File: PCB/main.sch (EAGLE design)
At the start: 38 parts, among them X1 BU-SMA-V

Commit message: Eagle Schematic From Lab
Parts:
- removed LSP1, LSP2: LSP10, solpad:LSP10
- added AUX-L, AUX-R, L-OUT, R-OUT, REC-L, REC-R: LSP10, solpad:LSP10
- added R10, R8, R9: 330, resistor:R-EU_M0805
- added R11, R12: 10k, resistor:R-EU_M0805
- added U$4, U$5: MAX4586, MAX4586:MAX4586
- JP4: device pinhead:PINHD-2X9 -> pinhead:PINHD-1X16
- renumbered LSP6 to V+, LSP7 to V-
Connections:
- net N$12 renamed D5
- net N$55 renamed V+
- removed net L-OUT: JP2.3, R7.1, U$1.L-OUT
- removed net N$14: JP4.16, U$2.RD7/SEG7
- removed net N$15: JP4.1, U$2.RF7/~SS/SEG25
- removed net N$16: JP4.3, U$2.RF6/AN11/SEG24
- removed net N$17: JP4.5, U$2.RF5/AN10/CVREF/SEG23
- removed net N$18: JP4.7, U$2.RF4/AN9/SEG22
- removed net N$19: JP4.9, U$2.RF3/AN8/SEG21
- removed net N$20: JP4.11, U$2.RF2/AN7/C1OUT/SEG20
- removed net N$21: JP4.13, U$2.RF1/AN6/C2OUT/SEG19
- removed net N$22: JP4.15, U$2.RF0/AN5/SEG18
- removed net N$5 (its old number): JP4.4, U$2.RD1/SEG1
- removed net N$52: JP9.3, U$2.RE6/COM3
- removed net N$53: JP9.4, U$2.RE7/CCP2/SEG31
- removed net N$54: U$2.COM0
- removed net N$57: R4.1, U$4.1.+IN
- removed net N$60: C6.1, C7.1, LSP1.MP
- removed net N$62: R7.2, U$4.2.+IN
- removed net N$64: C10.1, C9.1, LSP2.MP
- removed net N$67: JP1.2, R2.1, U$1.DATA
- removed net N$68: JP1.3, R1.1, U$1.CLOCK
- removed net N$7 (its old number): JP4.8, U$2.RD3/SEG3
- removed net R-OUT: JP2.2, R4.2, U$1.R-OUT
- new net AMP-L: U$4.COM
- new net AMP-R: U$5.COM
- new net AUX-L: AUX-L.MP, U$4.NO3
- new net AUX-R: AUX-R.MP, U$5.NO3
- new net COM0: JP9.1, U$2.COM0
- new net D0: JP4.7, U$2.RD0/SEG0
- new net D1: JP4.8, U$2.RD1/SEG1
- new net D2: JP4.9, U$2.RD2/SEG2
- new net D3: JP4.10
- new net D4: JP4.11, U$2.RD4/SEG4
- new net D6: JP4.13, U$2.RD6/SEG6
- new net D7: JP4.14, U$2.RD7/SEG7
- new net E: JP4.6, JP9.4, U$2.RE6/COM3
- new net FM-L: JP2.3, U$1.L-OUT, U$4.NO1
- new net FM-R: JP2.2, U$1.R-OUT, U$5.NO1
- new net REC-L: REC-L.MP, U$4.NO2
- new net REC-R: REC-R.MP, U$5.NO2
- new net RS: JP4.4, JP9.5, U$2.RE7/CCP2/SEG31
- net +3V3: now also JP4.2, R8.1, R9.2, U$4.A, U$4.V+, U$5.V+; no longer JP4.17
- net GND: now also JP4.1, JP4.16, JP4.5, R10.1, U$4.GND, U$5.A, U$5.GND; no longer JP4.18
- net N$13: now also JP4.3, R10.2, R9.1; no longer JP4.14, U$2.RD6/SEG6
- net N$2: now also JP4.15, R8.2; no longer JP4.2, U$2.RD0/SEG0
- net N$50: now also JP9.2; no longer JP9.1
- net N$51: now also JP9.3; no longer JP9.2
- net N$6: now also C10.1, C9.1, L-OUT.MP; no longer JP4.6, U$2.RD2/SEG2
- net N$8: now also C6.1, C7.1, R-OUT.MP; no longer JP4.10, U$2.RD4/SEG4
- net SCL: now also JP1.3, R1.1, U$1.CLOCK, U$4.SCL, U$5.SCL
- net SDA: now also JP1.2, R2.1, U$1.DATA, U$4.SDA, U$5.SDA
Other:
- note removed: "LCD screen"
- note removed: "Lout"
- note removed: "Rout"
- moved on the sheet: C1, C10, C2, C5, C6, C7, C8, C9, JP1, JP2, JP6, JP8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

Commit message: Eagle Schematic Changes
Pins numbers added
IC names added
Text re-aligned
Amp corrected
Components re-named
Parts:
- removed JP1, JP2: (no value), pinhead:PINHD-1X3
- removed JP3: (no value), pinhead:PINHD-1X6
- removed JP4: (no value), pinhead:PINHD-1X16
- removed JP5, JP6, JP7, JP8, JP9: (no value), pinhead:PINHD-1X8
- removed U$1: AR1010, ar1010:AR1010
- removed U$4.: TDA2822D, linear:TDA2822D
- removed U$5: MAX4586, MAX4586:MAX4586
- added AMP-: TDA2822D, linear:TDA2822D
- added H1: (no value), pinhead:PINHD-1X16
- added H2, H4, H5, H6, H7: (no value), pinhead:PINHD-1X8
- added H3: (no value), pinhead:PINHD-1X6
- added H8, H9: (no value), pinhead:PINHD-1X3
- added MICROCONTROLLER: PIC18F6490-I/PT, Microchip_By_element14_Batch_1:PIC18F6490-I/PT
- added VOLTAGE_REGULATOR: MCP1700T-1802E/TT, mcp1700t-vreg:MCP1700T-1802E/TT
- R11, R12: value 10k -> 330
- R4, R7: value 10k -> 100k
- R5: value 4.7 -> 10k
- R8: value 330 -> 10k
- R9: value 330 -> 4.7
- U$2: value PIC18F6490-I/PT -> AR1010; device Microchip_By_element14_Batch_1:PIC18F6490-I/PT -> ar1010:AR1010; VAL (none) -> AR1010
- U$3: value MCP1700T-1802E/TT -> MAX4586; device mcp1700t-vreg:MCP1700T-1802E/TT -> MAX4586:MAX4586; VAL (none) -> MAX4586
- U$4: VAL (none) -> MAX4586
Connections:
- removed net N$58: C5.1, U$4.1.-IN
- removed net N$65: C10.2, R6.1
- removed net N$66: C8.1, U$4.2.-IN
- new net N$12: AMP-R.-IN, C5.1
- new net N$14: AMP-L.-IN, C8.1
- new net N$16: C10.2, R9.2
- new net N$17: AMP-L.+IN, R7.2, R8.2
- new net N$8: AMP-R.+IN, R4.1, R5.2
- net +3V3: now also H1.2, H3.2, MICROCONTROLLER.AVDD, MICROCONTROLLER.VDD, MICROCONTROLLER.VDD_2, MICROCONTROLLER.VDD_3, MICROCONTROLLER.VDD_4, R10.1, R11.2, U$2.VCC, U$3.NO2, U$4.NO2, U$4.NO3, VOLTAGE_REGULATOR.VOUT; no longer JP3.2, JP4.2, R8.1, R9.2, U$1.VCC, U$2.AVDD, U$2.VDD, U$2.VDD_2, U$2.VDD_3, U$2.VDD_4, U$3.VOUT, U$4.A, U$4.V+, U$5.V+
- net AMP-L: now also R7.1, U$4.NO4; no longer U$4.COM
- net AMP-R: now also R4.2, U$3.NO4; no longer U$5.COM
- net AUX-L: now also U$4.A; no longer U$4.NO3
- net AUX-R: now also U$3.A; no longer U$5.NO3
- net COM0: now also H7.1, MICROCONTROLLER.COM0; no longer JP9.1, U$2.COM0
- net D0: now also H1.7, MICROCONTROLLER.RD0/SEG0; no longer JP4.7, U$2.RD0/SEG0
- net D1: now also H1.8, MICROCONTROLLER.RD1/SEG1; no longer JP4.8, U$2.RD1/SEG1
- net D2: now also H1.9, MICROCONTROLLER.RD2/SEG2; no longer JP4.9, U$2.RD2/SEG2
- net D3: now also H1.10, MICROCONTROLLER.RD3/SEG3; no longer JP4.10
- net D4: now also H1.11, MICROCONTROLLER.RD4/SEG4; no longer JP4.11, U$2.RD4/SEG4
- net D5: now also H1.12, MICROCONTROLLER.RD5/SEG5; no longer JP4.12, U$2.RD5/SEG5
- net D6: now also H1.13, MICROCONTROLLER.RD6/SEG6; no longer JP4.13, U$2.RD6/SEG6
- net D7: now also H1.14, MICROCONTROLLER.RD7/SEG7; no longer JP4.14, U$2.RD7/SEG7
- net E: now also H1.6, H7.4, MICROCONTROLLER.RE6/COM3; no longer JP4.6, JP9.4, U$2.RE6/COM3
- net FM-L: now also H8.3, U$2.L-OUT, U$4.SCL; no longer JP2.3, U$1.L-OUT, U$4.NO1
- net FM-R: now also H8.2, U$2.R-OUT, U$3.SCL; no longer JP2.2, U$1.R-OUT, U$5.NO1
- net GND: now also AMP-R.V-, H1.1, H1.16, H1.5, H3.3, H8.1, H9.1, MICROCONTROLLER.AVSS, MICROCONTROLLER.VSS, MICROCONTROLLER.VSS_2, MICROCONTROLLER.VSS_3, MICROCONTROLLER.VSS_4, R12.1, R6.1, R8.1, R9.1, U$2.BUSMODE, U$2.GND, U$3.NO3, U$3.SDA, U$4.SDA, VOLTAGE_REGULATOR.GND; no longer JP1.1, JP2.1, JP3.3, JP4.1, JP4.16, JP4.5, R10.1, R6.2, U$1.BUSMODE, U$1.GND, U$2.AVSS, U$2.VSS, U$2.VSS_2, U$2.VSS_3, U$2.VSS_4, U$3.GND, U$4.1.V-, U$4.GND, U$5.A, U$5.GND
- net N$1: now also H3.1, MICROCONTROLLER.RG5/~MCLR/VPP; no longer JP3.1, U$2.RG5/~MCLR/VPP
- net N$10: now also H3.5, H6.7, MICROCONTROLLER.RB6/KBI2/PGC; no longer JP3.5, JP5.7, U$2.RB6/KBI2/PGC
- net N$11: now also H3.4, H6.8, MICROCONTROLLER.RB7/KBI3/PGD; no longer JP3.4, JP5.8, U$2.RB7/KBI3/PGD
- net N$13: now also H1.3, R11.1, R12.2; no longer JP4.3, R10.2, R9.1
- net N$2: now also H1.15, R10.2; no longer JP4.15, R8.2
- net N$23: now also H5.8, MICROCONTROLLER.RC7/RX1/DT1; no longer JP6.8, U$2.RC7/RX1/DT1
- net N$24: now also H5.7, MICROCONTROLLER.RC6/TX1/CK1; no longer JP6.7, U$2.RC6/TX1/CK1
- net N$25: now also H6.5, MICROCONTROLLER.RB4/KBI0/SEG11; no longer JP5.5, U$2.RB4/KBI0/SEG11
- net N$26: now also H6.4, MICROCONTROLLER.RB3/INT3/SEG10; no longer JP5.4, U$2.RB3/INT3/SEG10
- net N$27: now also H6.3, MICROCONTROLLER.RB2/INT2/SEG9; no longer JP5.3, U$2.RB2/INT2/SEG9
- net N$28: now also H6.2, MICROCONTROLLER.RB1/INT1/SEG8; no longer JP5.2, U$2.RB1/INT1/SEG8
- net N$29: now also H6.1, MICROCONTROLLER.RB0/INT0; no longer JP5.1, U$2.RB0/INT0
- net N$3: now also U$2.W/R; no longer U$1.W/R
- net N$30: now also H5.6, MICROCONTROLLER.RC5/SDO/SEG12; no longer JP6.6, U$2.RC5/SDO/SEG12
- net N$31: now also H5.3, MICROCONTROLLER.RC2/CCP1/SEG13; no longer JP6.3, U$2.RC2/CCP1/SEG13
- net N$32: now also H5.2, MICROCONTROLLER.RC1/T1OSI/CCP2; no longer JP6.2, U$2.RC1/T1OSI/CCP2
- net N$33: now also H5.1, MICROCONTROLLER.RC0/T1OSO/T13CKI; no longer JP6.1, U$2.RC0/T1OSO/T13CKI
- net N$34: now also H4.8, MICROCONTROLLER.OSC1/CLKI/RA7; no longer JP7.8, U$2.OSC1/CLKI/RA7
- net N$35: now also H4.7, MICROCONTROLLER.OSC2/CLKO/RA6; no longer JP7.7, U$2.OSC2/CLKO/RA6
- net N$36: now also H4.6, MICROCONTROLLER.RA5/AN4/HLVDIN/SEG15; no longer JP7.6, U$2.RA5/AN4/HLVDIN/SEG15
- net N$37: now also H4.5, MICROCONTROLLER.RA4/T0CKI/SEG14; no longer JP7.5, U$2.RA4/T0CKI/SEG14
- net N$38: now also H4.4, MICROCONTROLLER.RA3/AN3/VREF+/SEG17; no longer JP7.4, U$2.RA3/AN3/VREF+/SEG17
- net N$39: now also H4.3, MICROCONTROLLER.RA2/AN2/VREF-/SEG16; no longer JP7.3, U$2.RA2/AN2/VREF-/SEG16
- net N$4: now also U$2.ANT; no longer U$1.ANT
- net N$40: now also H4.2, MICROCONTROLLER.RA1/AN1; no longer JP7.2, U$2.RA1/AN1
- net N$41: now also H4.1, MICROCONTROLLER.RA0/AN0; no longer JP7.1, U$2.RA0/AN0
- net N$42: now also H2.1, MICROCONTROLLER.RG4/SEG26; no longer JP8.1, U$2.RG4/SEG26
- net N$43: now also H2.2, MICROCONTROLLER.RG3/SEG27; no longer JP8.2, U$2.RG3/SEG27
- net N$44: now also H2.3, MICROCONTROLLER.RG2/RX2/DT2/SEG28; no longer JP8.3, U$2.RG2/RX2/DT2/SEG28
- net N$45: now also H2.4, MICROCONTROLLER.RG1/TX2/CK2/SEG29; no longer JP8.4, U$2.RG1/TX2/CK2/SEG29
- net N$46: now also H2.5, MICROCONTROLLER.RG0/SEG30; no longer JP8.5, U$2.RG0/SEG30
- net N$47: now also H2.6, MICROCONTROLLER.LCDBIAS3; no longer JP8.6, U$2.LCDBIAS3
- net N$48: now also H2.7, MICROCONTROLLER.LCDBIAS2; no longer JP8.7, U$2.LCDBIAS2
- net N$49: now also H2.8, MICROCONTROLLER.LCDBIAS1; no longer JP8.8, U$2.LCDBIAS1
- net N$5: now also AMP-L.OUT; no longer U$4.2.OUT
- net N$50: now also H7.2, MICROCONTROLLER.RE4/COM1; no longer JP9.2, U$2.RE4/COM1
- net N$51: now also H7.3, MICROCONTROLLER.RE5/COM2; no longer JP9.3, U$2.RE5/COM2
- net N$61: now also R6.2; no longer R5.2
- net N$7: now also AMP-R.OUT; no longer U$4.1.OUT
- net N$9: now also H6.6, MICROCONTROLLER.RB5/KBI1; no longer JP5.6, U$2.RB5/KBI1
- net REC-L: now also U$4.V+; no longer U$4.NO2
- net REC-R: now also U$3.V+; no longer U$5.NO2
- net RS: now also H1.4, H7.5, MICROCONTROLLER.RE7/CCP2/SEG31; no longer JP4.4, JP9.5, U$2.RE7/CCP2/SEG31
- net SCL: now also H5.4, H9.3, MICROCONTROLLER.RC3/SCK/SCL, U$2.CLOCK, U$3.NO1, U$4.NO1; no longer JP1.3, JP6.4, U$1.CLOCK, U$2.RC3/SCK/SCL, U$4.SCL, U$5.SCL
- net SDA: now also H5.5, H9.2, MICROCONTROLLER.RC4/SDI/SDA, U$2.DATA, U$3.GND, U$4.GND; no longer JP1.2, JP6.5, U$1.DATA, U$2.RC4/SDI/SDA, U$4.SDA, U$5.SDA
- net V+: now also AMP-R.V+, VOLTAGE_REGULATOR.VIN; no longer U$3.VIN, U$4.1.V+
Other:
- moved on the sheet: AUX-L, AUX-R, C1, C10, C2, C3, C4, C5, C6, C7, C8, C9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

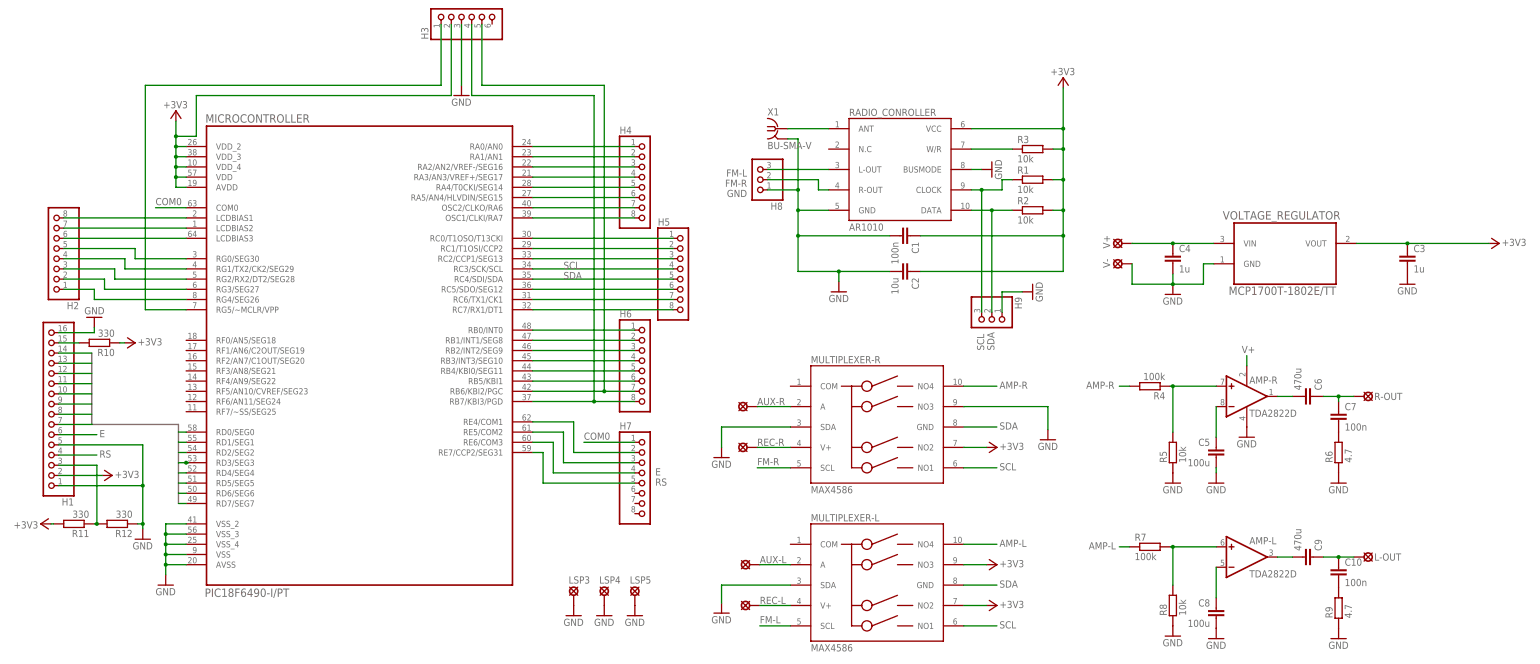
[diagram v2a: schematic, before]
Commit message: Eagle Schematic Changes
Fixed a few issues that didn't save properly.
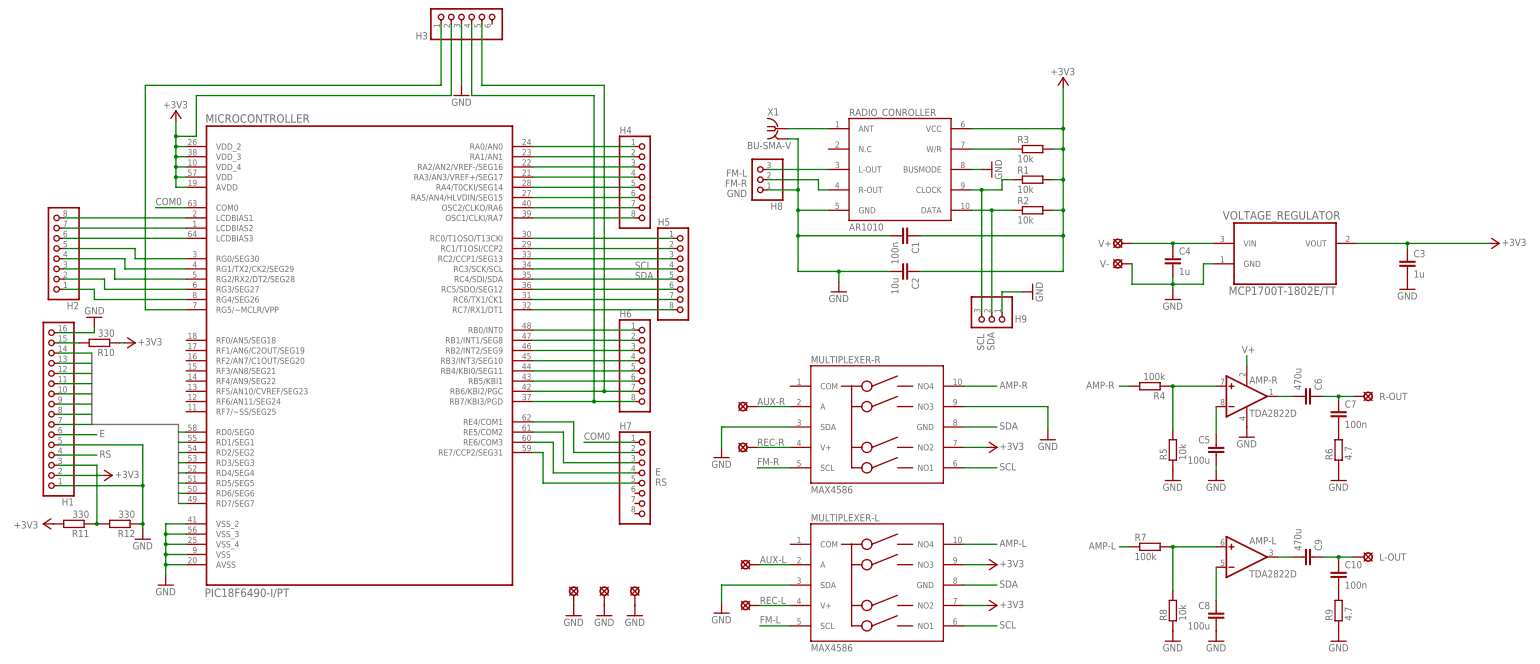
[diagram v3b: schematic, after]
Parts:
- renumbered LSP3 to G1, LSP4 to G2, LSP5 to G3
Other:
- moved on the sheet: C10, C3, C4, C5, C7, C8, R12, R5, R6, R8, R9

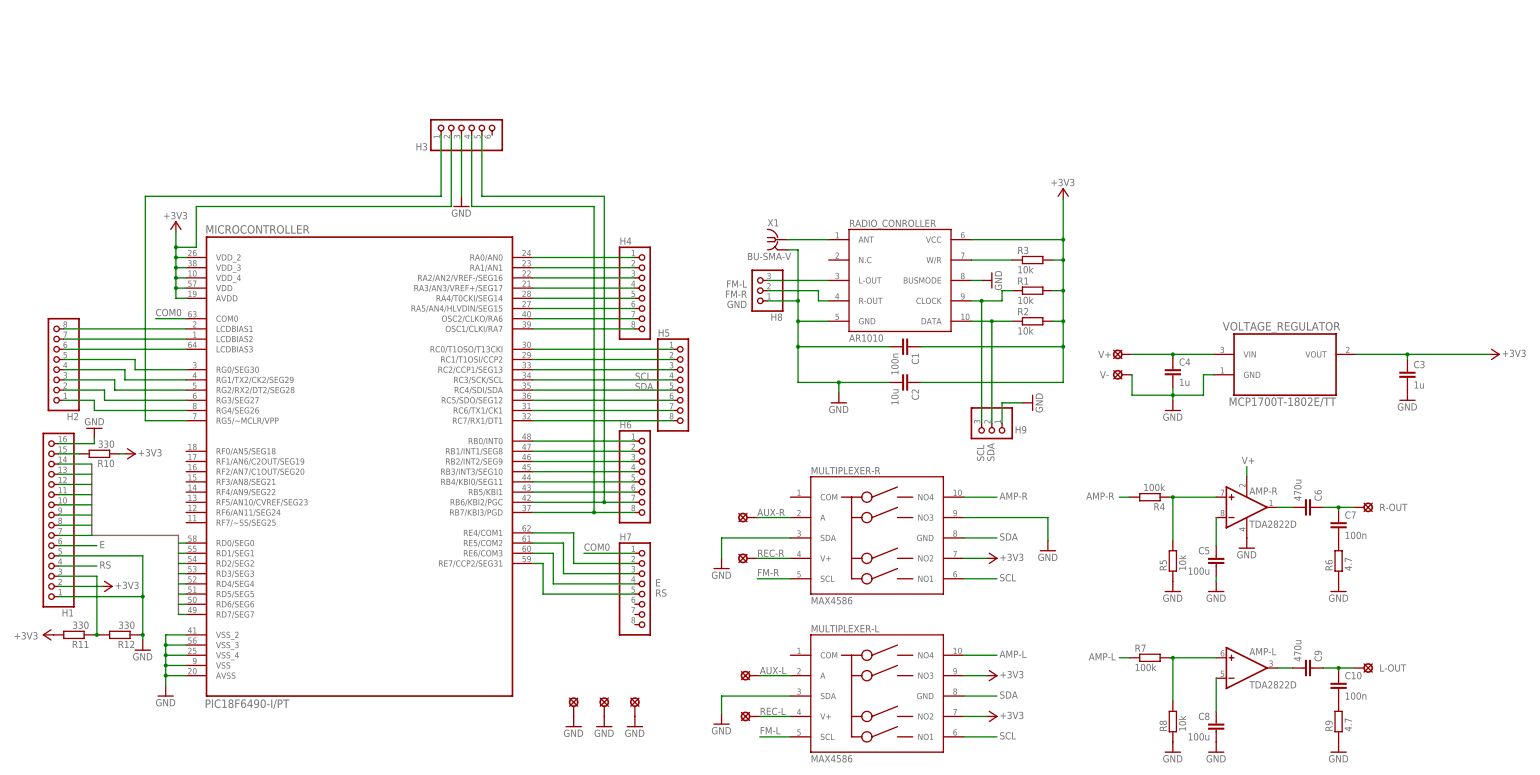
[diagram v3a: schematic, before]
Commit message: Eagle Schematic Changes
- Added V+, 3.3v and GND pads
- Split off ISCP, I2C and AUX connectors
- Various visual changes
- Added pull up resistor for MCLR
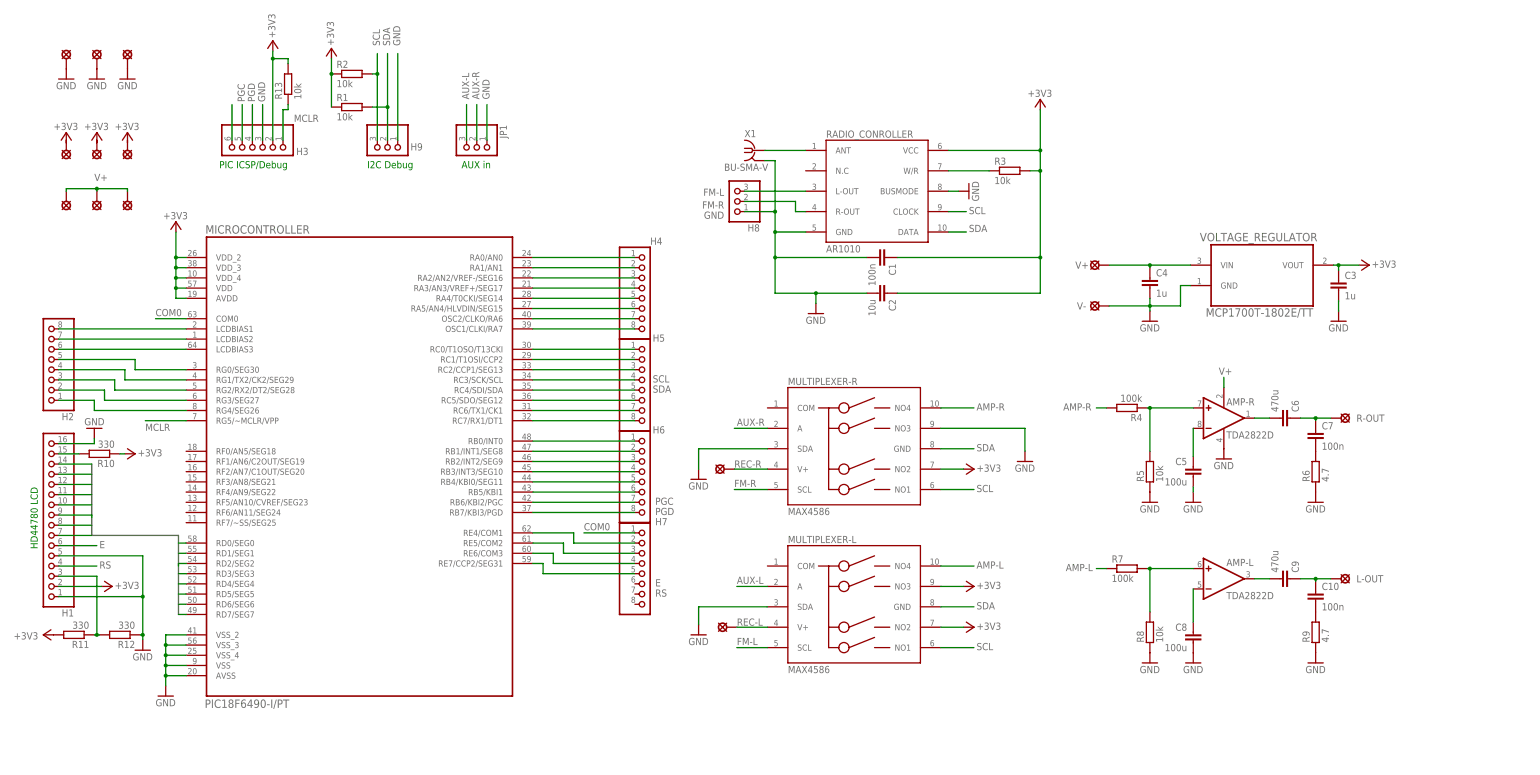
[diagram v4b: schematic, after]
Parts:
- removed AUX-L, AUX-R: LSP10, solpad:LSP10
- added G4, G5, G6, G7, G8, G9: LSP10, solpad:LSP10
- added JP1: (no value), pinhead:PINHD-1X3
- added R13: 10k, resistor:R-EU_M0805
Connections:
- net D0 renamed PORTD0
- net D1 renamed PORTD1
- net D2 renamed PORTD2
- net D3 renamed PORTD3
- net D4 renamed PORTD4
- net D5 renamed PORTD5
- net D6 renamed PORTD6
- net D7 renamed PORTD7
- net N$10 renamed PGC
- net N$11 renamed PGD
- removed net N$1: H3.1, MICROCONTROLLER.RG5/~MCLR/VPP
- new net MCLR: H3.1, MICROCONTROLLER.RG5/~MCLR/VPP, R13.1
- new net N$18: H3.6
- net +3V3: now also R1.1, R13.2, R2.1; no longer R1.2, R2.2
- net AUX-L: now also JP1.3; no longer AUX-L.MP
- net AUX-R: now also JP1.2; no longer AUX-R.MP
- net GND: now also JP1.1
- net SCL: now also R2.2; no longer R1.1
- net SDA: now also R1.2; no longer R2.1
- net V+: now also G7.MP, G8.MP, G9.MP
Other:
- note added: "AUX in"
- note added: "HD44780 LCD"
- note added: "I2C Debug"
- note added: "PIC ICSP/Debug"
- moved on the sheet: AMP-L, AMP-R, C1, C10, C2, C3, C4, C5, C6, C7, C8, C9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
